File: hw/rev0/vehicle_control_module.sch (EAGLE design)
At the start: 195 parts, among them IC1 SJA1105TELY, IC10 TJA1100HNZ, IC11 KSZ8061MNXI-TR, IC12 TJA1100HNZ, IC2 ATSAMV71Q21B-AABT, IC3 TJA1100HNZ, IC4 FT2232HL, IC5 TRS3232EQPWRQ1, IC6 SST26VF032BT-104I_SM, IC7 DS3231SN#, IC8 TLE9252VSKXUMA1, J1 2305018-2, J10 5-2337992-3, J12 1017505, J2 2305018-2, J3 1017505, J4 1017505, J5 1017505, J6 1017505, J7 1017505, J8 1017505, J9 1017505, U1 122-2920-GR, Y1 NX3225SA-25MHZ-EXS00A-CS11338, Y2 NX2016SA-25.000M-STD-CZS-1

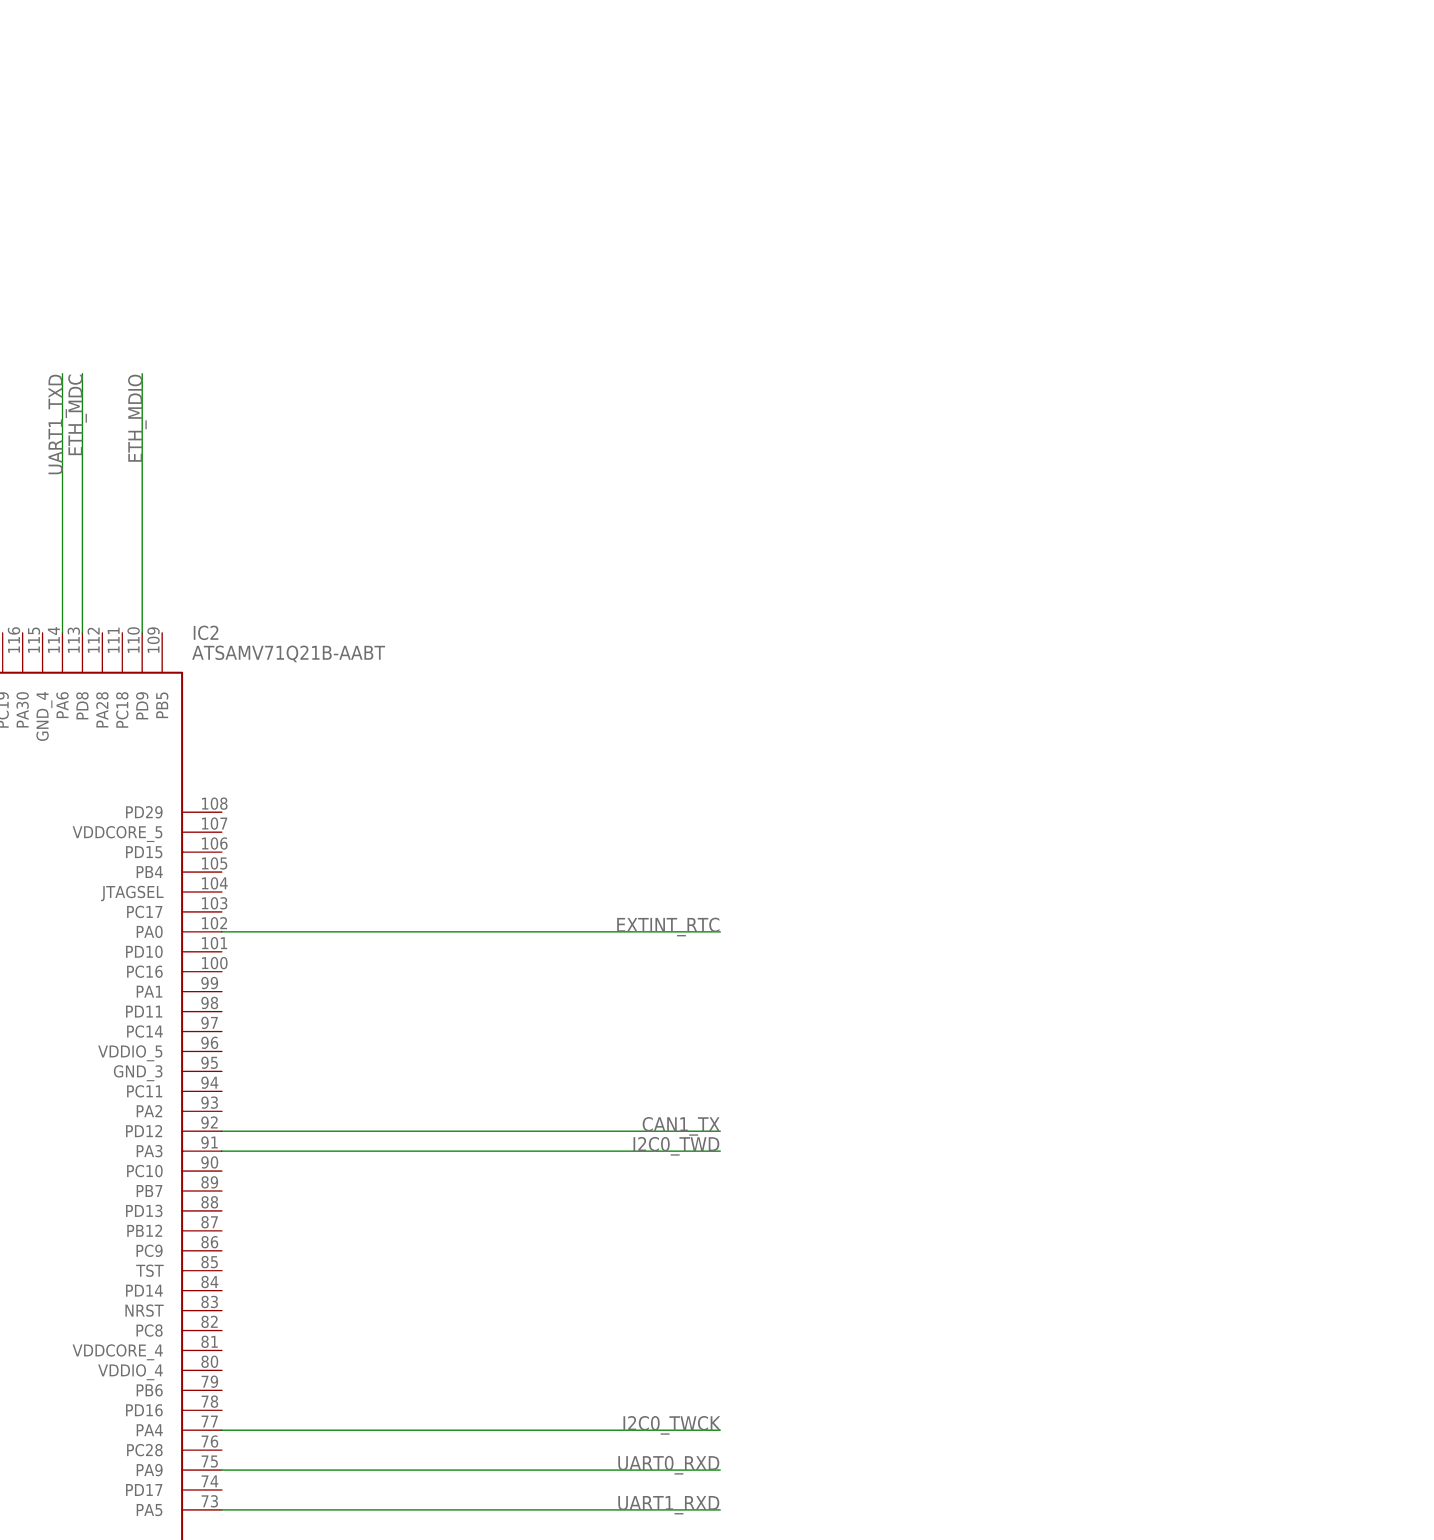
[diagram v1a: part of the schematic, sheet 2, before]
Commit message: Add JTAG connector
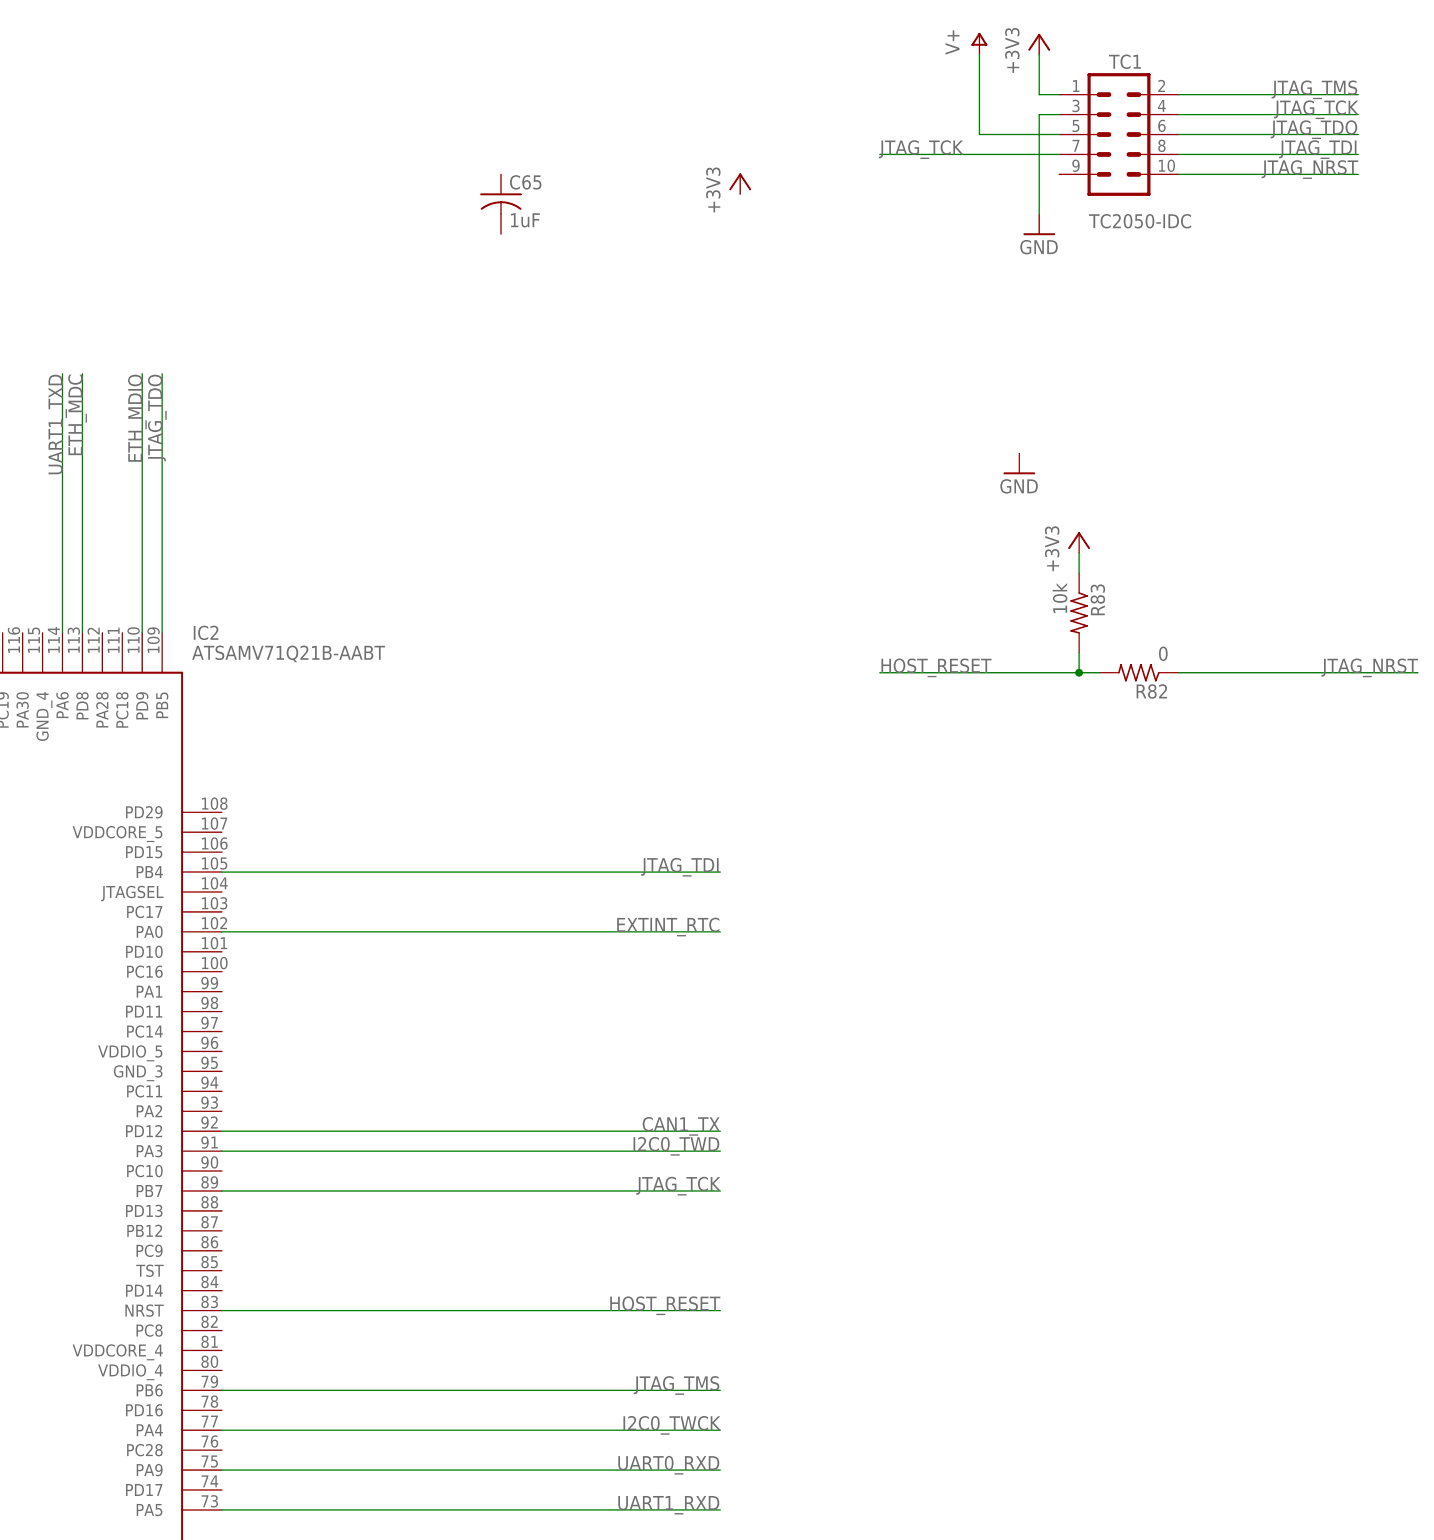
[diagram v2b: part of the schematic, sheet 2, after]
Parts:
- added C65: 1uF, rcl:C-USC0603
- added R82: 0, rcl:R-US_R0603
- added R83: 10k, rcl:R-US_R0603
- added TC1: TC2050-IDC, TagConnect:TC2050-IDC
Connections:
- new net HOST_RESET: IC2.NRST, R82.2, R83.2
- new net JTAG_NRST: R82.1, TC1.10
- new net JTAG_TCK: IC2.PB7, TC1.4, TC1.7
- new net JTAG_TDI: IC2.PB4, TC1.8
- new net JTAG_TDO: IC2.PB5, TC1.6
- new net JTAG_TMS: IC2.PB6, TC1.2
- new net V+: TC1.5
- net +3V3: now also R83.1, TC1.1
- net GND: now also TC1.3
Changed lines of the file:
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@@
 <layer number="48" name="Document" color="7" fill="1" visible="no" active="no"/>
 <layer number="49" name="Reference" color="7" fill="1" visible="no" active="no"/>
+<layer number="50" name="dxf" color="7" fill="1" visible="no" active="no"/>
 <layer number="51" name="tDocu" color="7" fill="1" visible="no" active="no"/>
 <layer number="52" name="bDocu" color="7" fill="1" visible="no" active="no"/>
@@
 <layer number="97" name="Info" color="7" fill="1" visible="yes" active="yes"/>
 <layer number="98" name="Guide" color="6" fill="1" visible="yes" active="yes"/>
+<layer number="200" name="200bmp" color="1" fill="10" visible="no" active="no"/>
+<layer number="250" name="Descript" color="3" fill="1" visible="no" active="no"/>
+<layer number="251" name="SMDround" color="12" fill="11" visible="no" active="no"/>
 </layers>
 <schematic xreflabel="%F%N/%S.%C%R" xrefpart="/%S.%C%R">
@@
 <part name="GND107" library="supply1" library_urn="urn:adsk.eagle:library:371" deviceset="GND" device=""/>
 <part name="+3V48" library="supply1" library_urn="urn:adsk.eagle:library:371" deviceset="+3V3" device=""/>
+<part name="C65" library="rcl" library_urn="urn:adsk.eagle:library:334" deviceset="C-US" device="C0603" package3d_urn="urn:adsk.eagle:package:23616/2" value="1uF"/>
+<part name="R82" library="rcl" library_urn="urn:adsk.eagle:library:334" deviceset="R-US_" device="R0603" package3d_urn="urn:adsk.eagle:package:23555/3" value="0"/>
+<part name="GND108" library="supply1" library_urn="urn:adsk.eagle:library:371" deviceset="GND" device=""/>
+<part name="+3V49" library="supply1" library_urn="urn:adsk.eagle:library:371" deviceset="+3V3" device=""/>
+<part name="+3V50" library="supply1" library_urn="urn:adsk.eagle:library:371" deviceset="+3V3" device=""/>
+<part name="GND109" library="supply1" library_urn="urn:adsk.eagle:library:371" deviceset="GND" device=""/>
+<part name="R83" library="rcl" library_urn="urn:adsk.eagle:library:334" deviceset="R-US_" device="R0603" package3d_urn="urn:adsk.eagle:package:23555/3" value="10k"/>
+<part name="+3V51" library="supply1" library_urn="urn:adsk.eagle:library:371" deviceset="+3V3" device=""/>
+<part name="TC1" library="TagConnect" deviceset="TC2050-IDC" device=""/>
+<part name="P+1" library="supply1" library_urn="urn:adsk.eagle:library:371" deviceset="V+" device=""/>
 </parts>
 <sheets>
@@
 <attribute name="DRAWING_NAME" x="342.9" y="19.05" size="2.54" layer="94"/>
 </instance>
+<instance part="C65" gate="G$1" x="251.46" y="233.68" smashed="yes">
+<attribute name="NAME" x="252.476" y="234.315" size="1.778" layer="95"/>
+<attribute name="VALUE" x="252.476" y="229.489" size="1.778" layer="96"/>
+</instance>
+<instance part="R82" gate="G$1" x="332.74" y="172.72" smashed="yes" rot="R180">
+<attribute name="NAME" x="336.55" y="171.2214" size="1.778" layer="95" rot="R180"/>
+<attribute name="VALUE" x="336.55" y="176.022" size="1.778" layer="96" rot="R180"/>
+</instance>
+<instance part="GND108" gate="1" x="320.04" y="228.6" smashed="yes">
+<attribute name="VALUE" x="317.5" y="226.06" size="1.778" layer="96"/>
+</instance>
+<instance part="+3V49" gate="G$1" x="281.94" y="236.22" smashed="yes">
+<attribute name="VALUE" x="279.4" y="231.14" size="1.778" layer="96" rot="R90"/>
+</instance>
+<instance part="+3V50" gate="G$1" x="320.04" y="254" smashed="yes">
+<attribute name="VALUE" x="317.5" y="248.92" size="1.778" layer="96" rot="R90"/>
+</instance>
+<instance part="GND109" gate="1" x="317.5" y="198.12" smashed="yes">
+<attribute name="VALUE" x="314.96" y="195.58" size="1.778" layer="96"/>
+</instance>
+<instance part="R83" gate="G$1" x="325.12" y="180.34" smashed="yes" rot="R270">
+<attribute name="NAME" x="326.6186" y="184.15" size="1.778" layer="95" rot="R270"/>
+<attribute name="VALUE" x="321.818" y="184.15" size="1.778" layer="96" rot="R270"/>
+</instance>
+<instance part="+3V51" gate="G$1" x="325.12" y="190.5" smashed="yes">
+<attribute name="VALUE" x="322.58" y="185.42" size="1.778" layer="96" rot="R90"/>
+</instance>
+<instance part="TC1" gate="A" x="330.2" y="241.3" smashed="yes" rot="R180">
+<attribute name="VALUE" x="326.39" y="231.14" size="1.778" layer="96" rot="MR180"/>
+<attribute name="NAME" x="328.93" y="249.682" size="1.778" layer="95"/>
+</instance>
+<instance part="P+1" gate="1" x="312.42" y="254" smashed="yes">
+<attribute name="VALUE" x="309.88" y="251.46" size="1.778" layer="96" rot="R90"/>
+</instance>
 </instances>
 <busses>
@@
 </segment>
 </net>
+<net name="+3V3" class="0">
+<segment>
+<pinref part="R83" gate="G$1" pin="1"/>
+<pinref part="+3V51" gate="G$1" pin="+3V3"/>
+<wire x1="325.12" y1="187.96" x2="325.12" y2="185.42" width="0.1524" layer="91"/>
+</segment>
+<segment>
+<pinref part="TC1" gate="A" pin="1"/>
+<wire x1="322.58" y1="246.38" x2="320.04" y2="246.38" width="0.1524" layer="91"/>
+<pinref part="+3V50" gate="G$1" pin="+3V3"/>
+<wire x1="320.04" y1="246.38" x2="320.04" y2="251.46" width="0.1524" layer="91"/>
+</segment>
+</net>
+<net name="JTAG_TMS" class="0">
+<segment>
+<pinref part="IC2" gate="G$1" pin="PB6"/>
+<wire x1="215.9" y1="81.28" x2="279.4" y2="81.28" width="0.1524" layer="91"/>
+<label x="279.4" y="81.28" size="1.778" layer="95" rot="MR0"/>
+</segment>
+<segment>
+<pinref part="TC1" gate="A" pin="2"/>
+<wire x1="337.82" y1="246.38" x2="360.68" y2="246.38" width="0.1524" layer="91"/>
+<label x="360.68" y="246.38" size="1.778" layer="95" rot="MR0"/>
+</segment>
+</net>
+<net name="JTAG_TCK" class="0">
+<segment>
+<pinref part="IC2" gate="G$1" pin="PB7"/>
+<wire x1="215.9" y1="106.68" x2="279.4" y2="106.68" width="0.1524" layer="91"/>
+<label x="279.4" y="106.68" size="1.778" layer="95" rot="MR0"/>
+</segment>
+<segment>
+<pinref part="TC1" gate="A" pin="4"/>
+<wire x1="337.82" y1="243.84" x2="360.68" y2="243.84" width="0.1524" layer="91"/>
+<label x="360.68" y="243.84" size="1.778" layer="95" rot="MR0"/>
+</segment>
+<segment>
+<pinref part="TC1" gate="A" pin="7"/>
+<wire x1="322.58" y1="238.76" x2="299.72" y2="238.76" width="0.1524" layer="91"/>
+<label x="299.72" y="238.76" size="1.778" layer="95"/>
+</segment>
+</net>
+<net name="JTAG_TDO" class="0">
+<segment>
+<pinref part="IC2" gate="G$1" pin="PB5"/>
+<wire x1="208.28" y1="177.8" x2="208.28" y2="210.82" width="0.1524" layer="91"/>
+<label x="208.28" y="210.82" size="1.778" layer="95" rot="MR270"/>
+</segment>
+<segment>
+<pinref part="TC1" gate="A" pin="6"/>
+<wire x1="337.82" y1="241.3" x2="360.68" y2="241.3" width="0.1524" layer="91"/>
+<label x="360.68" y="241.3" size="1.778" layer="95" rot="MR0"/>
+</segment>
+</net>
+<net name="JTAG_TDI" class="0">
+<segment>
+<pinref part="IC2" gate="G$1" pin="PB4"/>
+<wire x1="215.9" y1="147.32" x2="279.4" y2="147.32" width="0.1524" layer="91"/>
+<label x="279.4" y="147.32" size="1.778" layer="95" rot="MR0"/>
+</segment>
+<segment>
+<pinref part="TC1" gate="A" pin="8"/>
+<wire x1="337.82" y1="238.76" x2="360.68" y2="238.76" width="0.1524" layer="91"/>
+<label x="360.68" y="238.76" size="1.778" layer="95" rot="MR0"/>
+</segment>
+</net>
+<net name="JTAG_NRST" class="0">
+<segment>
+<pinref part="R82" gate="G$1" pin="1"/>
+<wire x1="337.82" y1="172.72" x2="368.3" y2="172.72" width="0.1524" layer="91"/>
+<label x="368.3" y="172.72" size="1.778" layer="95" rot="MR0"/>
+</segment>
+<segment>
+<pinref part="TC1" gate="A" pin="10"/>
+<wire x1="337.82" y1="236.22" x2="360.68" y2="236.22" width="0.1524" layer="91"/>
+<label x="360.68" y="236.22" size="1.778" layer="95" rot="MR0"/>
+</segment>
+</net>
+<net name="HOST_RESET" class="0">
+<segment>
+<pinref part="IC2" gate="G$1" pin="NRST"/>
+<wire x1="215.9" y1="91.44" x2="279.4" y2="91.44" width="0.1524" layer="91"/>
+<label x="279.4" y="91.44" size="1.778" layer="95" rot="MR0"/>
+</segment>
+<segment>
+<pinref part="R82" gate="G$1" pin="2"/>
+<wire x1="327.66" y1="172.72" x2="325.12" y2="172.72" width="0.1524" layer="91"/>
+<pinref part="R83" gate="G$1" pin="2"/>
+<wire x1="325.12" y1="172.72" x2="299.72" y2="172.72" width="0.1524" layer="91"/>
+<wire x1="325.12" y1="175.26" x2="325.12" y2="172.72" width="0.1524" layer="91"/>
+<junction x="325.12" y="172.72"/>
+<label x="299.72" y="172.72" size="1.778" layer="95"/>
+</segment>
+</net>
+<net name="GND" class="0">
+<segment>
+<pinref part="TC1" gate="A" pin="3"/>
+<wire x1="322.58" y1="243.84" x2="320.04" y2="243.84" width="0.1524" layer="91"/>
+<pinref part="GND108" gate="1" pin="GND"/>
+<wire x1="320.04" y1="243.84" x2="320.04" y2="231.14" width="0.1524" layer="91"/>
+</segment>
+</net>
+<net name="V+" class="0">
+<segment>
+<pinref part="TC1" gate="A" pin="5"/>
+<wire x1="322.58" y1="241.3" x2="312.42" y2="241.3" width="0.1524" layer="91"/>
+<pinref part="P+1" gate="1" pin="V+"/>
+<wire x1="312.42" y1="241.3" x2="312.42" y2="251.46" width="0.1524" layer="91"/>
+</segment>
+</net>

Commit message: Flesh out FTDI and RS232
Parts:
- added C66, C68, C69, C70, C75, C76, C77, C78: 100nF, rcl:C-USC0603
- added C67: 3.3uF, rcl:C-USC0603
- added C71, C72: 4.7uF, rcl:C-USC0603
- added C73, C74: 18nF, rcl:C-USC0603
- added C79, C80, C81, C82: 0.1uF, rcl:C-USC0603
- added J11, J13: 2301843-1, samacsys:2301843-1
- added LED4, LED5, LED6, LED7: (no value), led:LEDCHIPLED_0603
- added R84: 10k, rcl:R-US_R0603
- added R85, R88, R89, R90, R91, R92: 12k, rcl:R-US_R0603
- added R86, R87: 5.11k, rcl:R-US_R0603
- added Y3: ABM8AIG-12.000MHZ-1Z-T, samacsys:ABM8AIG-12.000MHZ-1Z-T
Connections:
- new net DEBUG_USB_DM: IC4.DM, J2.DA_N, J2.DB_N
- new net DEBUG_USB_DP: IC4.DP, J2.DA_P, J2.DB_P
- new net FTDI_OSCI: C74.1, IC4.OSCI, Y3.CRYSTAL_2
- new net FTDI_OSCO: C73.1, IC4.OSCO, Y3.CRYSTAL_1
- new net N$67: J2.CC1, R86.2
- new net N$68: J2.CC2, R87.2
- new net N$69: IC4.REF, R85.1
- new net N$70: IC4.RESET#, R88.2
- new net N$71: LED5.A, R90.2
- new net N$72: LED4.A, R89.2
- new net N$73: LED6.A, R91.2
- new net N$74: LED7.A, R92.2
- new net N$75: C79.1, IC5.C1+
- new net N$76: C79.2, IC5.C1-
- new net N$77: C80.1, IC5.C2+
- new net N$78: C80.2, IC5.C2-
- new net N$79: C81.1, IC5.V-
- new net RS232_PORT0_RX: IC5.RIN1, J11.2
- new net RS232_PORT0_TX: IC5.DOUT1, J11.3
- new net RS232_PORT1_RX: IC5.RIN2, J13.2
- new net RS232_PORT1_TX: IC5.DOUT2, J13.3
- new net UART0_RX_LED: IC4.ACBUS3, R89.1
- new net UART0_TX_LED: IC4.ACBUS4, R90.1
- new net UART1_RX_LED: IC4.BCBUS3, R91.1
- new net UART1_TX_LED: IC4.BCBUS4, R92.1
- new net VEE: C67.1, C68.1, C69.1, C70.1, IC4.VCORE_1, IC4.VCORE_2, IC4.VCORE_3, IC4.VREGOUT
- net +3V3: now also C66.1, C71.1, C72.1, C75.1, C76.1, C77.1, C78.1, C82.1, IC4.VCCIO_1, IC4.VCCIO_2, IC4.VCCIO_3, IC4.VCCIO_4, IC4.VPHY, IC4.VPLL, IC4.VREGIN, IC5.VCC, R88.1
- net GND: now also C66.2, C67.2, C68.2, C69.2, C70.2, C71.2, C72.2, C73.2, C74.2, C75.2, C76.2, C77.2, C78.2, C81.2, C82.2, IC4.AGND, IC4.GND_1, IC4.GND_2, IC4.GND_3, IC4.GND_4, IC4.GND_5, IC4.GND_6, IC4.GND_7, IC4.GND_8, IC4.TEST, IC5.GND, J1.GND, J1.GNDA, J1.GNDB, J1.SHIELD, J11.5, J11.MH1, J11.MH2, J13.5, J13.MH1, J13.MH2, J2.GND, J2.GNDA, J2.GNDB, J2.SHIELD, LED4.C, LED5.C, LED6.C, LED7.C, R1.1, R2.1, R85.2, R86.1, R87.1, Y3.GND_1, Y3.GND_2
- net UART0_RXD: now also IC4.ADBUS0
- net UART0_TXD: now also IC4.ADBUS1
- net UART1_RXD: now also IC4.BDBUS0
- net UART1_TXD: now also IC4.BDBUS1
- net UART2_RXD: now also IC5.ROUT1
- net UART2_TXD: now also IC5.DIN1
- net UART3_RXD: now also IC5.ROUT2
- net UART3_TXD: now also IC5.DIN2
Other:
- note added: "10. High Side Drivers"
- note added: "11. CAN"
- note added: "12. Connectors"
- note added: "3. RS232 and Debug UART"
- note added: "4. External Flash and RTC"
- note added: "5. Ethernet Switch"
- note added: "6. Ethernet PHY 1"
- note added: "7. Ethernet PHY 2"
- note added: "8. Ethernet PHY 3"
- note added: "9. Ethernet PHY 4"
- note removed: "ETHERNET PHY 1"
- note removed: "ETHERNET PHY 2"
- note removed: "ETHERNET PHY 3"
- note removed: "ETHERNET PHY 4"

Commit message: Start adding power supply
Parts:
- added C83, C88: 0.47uF, rcl:C-USC0805
- added C84, C85: 470pF, rcl:C-USC0603
- added C86: UCZ1K151MNQ1MS, samacsys:UCZ1K151MNQ1MS
- added C87: 10uF, rcl:C-USC0805
- added D4, D5: PMEG3030EP,115, samacsys:PMEG3030EP,115
- added D7: SMAJ24CA-Q, samacsys:SMAJ24CA-Q
- added IC13: TPS79133MDBVTEP, samacsys:TPS79133MDBVTEP
- added IC9: TPS62242DRVR, samacsys:TPS62242DRVR
- added L7: XAL4020-102MEC, samacsys:XAL4020-102MEC
- added R93: 10k, rcl:R-US_R0603
- added U2: LM63625, LM63625:LM63625DQPWPRQ1PWP0016K_L
- added U3: TPS62007-Q1_DGS_10, TPS62007:TPS62007-Q1_DGS_10
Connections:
- removed net V+: TC1.5
- new net EXT_PWR: D5.A, TC1.5
- new net HOST_USB_VBUS: J1.VBUS_A, J1.VBUS_B
- new net N$80: C83.1, D4.K, D5.K, L7.1
- new net N$81: C84.2, C85.1
- new net N$82: C86.+, C87.1, C88.1, L7.2, U2.VIN, U2.VIN_2
- new net VBATT: C84.1, D4.A, D7.2
- net GND: now also C83.2, C85.2, C86.-, C87.2, C88.2, D7.1
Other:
- note added: "1V2 for Ethernet Switch"
- note added: "3.3V for Main Power"
- note added: "3V3 for analog reference"
- note added: "Vbatt to 5V"
